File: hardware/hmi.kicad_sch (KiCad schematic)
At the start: 21 parts, among them J4 Conn_01x08, Q1 PNP, Q2 NPN, SW1 SW_Push, SW2 SW_Push, SW3 SW_Push, SW4 SW_Push, SW5 SW_Push, SW6 SW_Push, SW7 SW_Push, U8 PCF8574

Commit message: Second revision of schematic
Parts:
- removed C12: 4u7, symbol Device:C
- removed RN1: 9 x 10k, Resistor_THT:R_Array_SIP10, symbol Device:R_Network09
- removed U8: PCF8574, symbol Interface_Expansion:PCF8574
- added C12: 4u7, Capacitor_THT:CP_Radial_D4.0mm_P2.00mm, symbol Device:C_Polarized
- added J4, J5: Conn_01x07, Connector_PinHeader_2.54mm:PinHeader_1x07_P2.54mm_Vertical, symbol Connector_Generic:Conn_01x07
- added U8: PCF8574T, Package_SO:SOIC-16W_7.5x10.3mm_P1.27mm, symbol Interface_Expansion:PCF8574T
- BZ1: footprint (none) -> Connector_PinHeader_2.54mm:PinHeader_1x02_P2.54mm_Vertical
- D5: renamed from D4; footprint (none) -> LED_SMD:LED_1206_3216Metric
- J6: renamed from J4; footprint (none) -> Connector_PinHeader_2.54mm:PinHeader_1x08_P2.54mm_Vertical
- Q1, Q2: footprint (none) -> Package_TO_SOT_SMD:SOT-23
- R24: renamed from R22; footprint (none) -> Resistor_SMD:R_0603_1608Metric
- R25: renamed from R24; footprint (none) -> Resistor_SMD:R_0603_1608Metric
- R26: renamed from R23; footprint (none) -> Resistor_SMD:R_0603_1608Metric
- R27: renamed from R25; footprint (none) -> Resistor_SMD:R_0603_1608Metric
- R28: renamed from R26; footprint (none) -> Resistor_SMD:R_0603_1608Metric
- RV1: footprint (none) -> Potentiometer_SMD:Potentiometer_Vishay_TS53YJ_Vertical
- SW2: renamed from SW1; footprint (none) -> Button_Switch_SMD:SW_SPST_TL3342
- SW3: renamed from SW2; footprint (none) -> Button_Switch_SMD:SW_SPST_TL3342
- SW4: renamed from SW3; footprint (none) -> Button_Switch_SMD:SW_SPST_TL3342
- SW5: renamed from SW4; footprint (none) -> Button_Switch_SMD:SW_SPST_TL3342
- SW6: renamed from SW5; footprint (none) -> Button_Switch_SMD:SW_SPST_TL3342
- SW7: renamed from SW6; footprint (none) -> Button_Switch_SMD:SW_SPST_TL3342
- SW8: renamed from SW7; footprint (none) -> Button_Switch_SMD:SW_SPST_TL3342
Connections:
- net +5V is gone; now on net GND: D5.1 (K)
- net +3.3V: now also U8.16 (VDD)
- net A_Button: now also J5.1 (Pin_1)
- net B_Button: now also J5.2 (Pin_2)
- net C_Button: now also J5.3 (Pin_3)
- net GND: now also C12.2, U8.1 (A0), U8.2 (A1), U8.3 (A2), U8.8 (GND)
- net LCD_RST: now also C12.1
- net Left_Button: now also J5.5 (Pin_5)
- net POWER_EN: now also U8.4 (P0)
- net Right_Button: now also J5.4 (Pin_4)
- net SCL: now also U8.14 (SCL)
- net SDA: now also U8.15 (SDA)
- net Down renamed Down_Button
- net Down_Button: now also J5.6 (Pin_6)
- net UP renamed UP_Button
- net UP_Button: now also J5.7 (Pin_7)
- new net A_Button_CONN: J4.1 (Pin_1), U8.5 (P1)
- new net B_Button_CONN: J4.2 (Pin_2), U8.6 (P2)
- new net C_Button_CONN: J4.3 (Pin_3), U8.7 (P3)
- new net Down_Button_CONN: J4.6 (Pin_6), U8.11 (P6)
- new net Left_Button_CONN: J4.5 (Pin_5), U8.10 (P5)
- new net Right_Button_CONN: J4.4 (Pin_4), U8.9 (P4)
- new net UP_Button_CONN: J4.7 (Pin_7), U8.12 (P7)
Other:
- moved on the sheet: D5, J6, Q1, R25, R26, R27

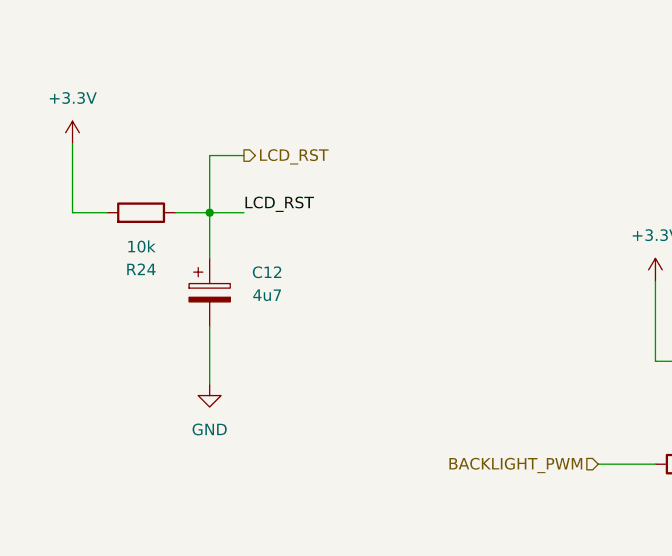
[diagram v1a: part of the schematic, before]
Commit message: Initial PCB placement and some schematic changes
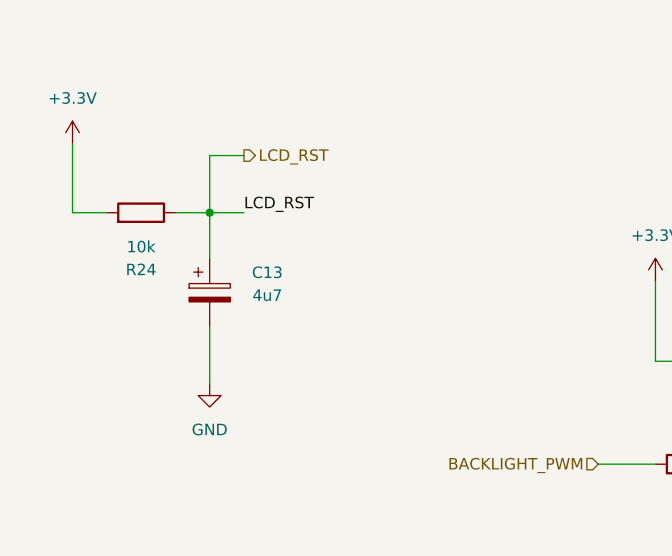
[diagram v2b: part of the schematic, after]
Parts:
- D5: footprint LED_SMD:LED_1206_3216Metric -> Diode_SMD:D_0603_1608Metric_Pad1.05x0.95mm_HandSolder
- renumbered C12 to C13
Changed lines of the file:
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@@
 			)
 		)
-		(property "Footprint" "LED_SMD:LED_1206_3216Metric"
+		(property "Footprint" "Diode_SMD:D_0603_1608Metric_Pad1.05x0.95mm_HandSolder"
 			(at 140.97 153.67 0)
 			(effects
@@
 		(on_board yes)
 		(dnp no)
-		(property "Reference" "C12"
+		(property "Reference" "C13"
 			(at 58.4835 49.8475 0)
 			(effects
@@
 			(project "esp8266_pygame"
 				(path "/fc3c54fb-6d1c-4231-9293-8fcb9c0b9706/4d35df8b-f9a9-4663-8ccd-4f07537e2734"
-					(reference "C12")
-					(unit 1)
-				)
+					(reference "C13")
+					(unit 1)
+				)

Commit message: Fixed keypad connector
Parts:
- removed J4, J5: Conn_01x07, Connector_PinHeader_2.54mm:PinHeader_1x07_P2.54mm_Vertical, symbol Connector_Generic:Conn_01x07
- added J4, J5: Conn_01x08, Connector_PinSocket_2.54mm:PinSocket_1x08_P2.54mm_Vertical, symbol Connector_Generic:Conn_01x08
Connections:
- net A_Button: now also J5.1 (Pin_1)
- net A_Button_CONN: now also J4.1 (Pin_1)
- net B_Button: now also J5.2 (Pin_2)
- net B_Button_CONN: now also J4.2 (Pin_2)
- net C_Button: now also J5.3 (Pin_3)
- net C_Button_CONN: now also J4.3 (Pin_3)
- net Down_Button: now also J5.6 (Pin_6)
- net Down_Button_CONN: now also J4.6 (Pin_6)
- net GND: now also J4.8 (Pin_8); no longer SW2.2, SW3.2, SW4.2, SW5.2, SW6.2, SW7.2, SW8.2
- net Left_Button: now also J5.5 (Pin_5)
- net Left_Button_CONN: now also J4.5 (Pin_5)
- net Right_Button: now also J5.4 (Pin_4)
- net Right_Button_CONN: now also J4.4 (Pin_4)
- net UP_Button: now also J5.7 (Pin_7)
- net UP_Button_CONN: now also J4.7 (Pin_7)
- new net BTN_GND: J5.8 (Pin_8), SW2.2, SW3.2, SW4.2, SW5.2, SW6.2, SW7.2, SW8.2

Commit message: Audio improvements
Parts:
- removed Q2: NPN, Package_TO_SOT_SMD:SOT-23, symbol Simulation_SPICE:NPN
- added C13: 100n, Capacitor_SMD:C_0603_1608Metric, symbol Device:C
- added C14: 10n, Capacitor_SMD:C_0603_1608Metric, symbol Device:C
- added C15: 10u, Capacitor_THT:CP_Radial_D4.0mm_P2.00mm, symbol Device:C_Polarized
- added C16: 47n, Capacitor_SMD:C_0603_1608Metric, symbol Device:C
- added C17: 220u, Capacitor_THT:CP_Radial_D4.0mm_P2.00mm, symbol Device:C_Polarized
- added R29: 10k, Resistor_SMD:R_0603_1608Metric, symbol Device:R
- added R30: 10, Resistor_SMD:R_0603_1608Metric, symbol Device:R
- added U9: LM386, Package_SO:SO-8_3.9x4.9mm_P1.27mm, symbol Amplifier_Audio:LM386
- renumbered C13 to C12
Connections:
- net +3.3V: no longer BZ1.1 (-)
- net BTN_GND: now also J5.5 (Pin_5); no longer J5.8 (Pin_8)
- net BUZZER: now also R28.1; no longer RV1.2
- net GND: now also BZ1.2 (+), J4.5 (Pin_5), C13.1, C14.1, R30.2, U9.2 (-), U9.4 (GND); no longer J4.8 (Pin_8)
- net Left_Button: now also J5.8 (Pin_8); no longer J5.5 (Pin_5)
- net Left_Button_CONN: now also J4.8 (Pin_8); no longer J4.5 (Pin_5)
- net at RV1.3: now also U9.3 (+); no longer R28.1
- net at R28.2: now also C13.2, R29.1
- new net: C14.2, R29.2, RV1.2
- new net: C16.2, C17.1, U9.5
- new net: BZ1.1 (-), C17.2
- new net: C15.1, U9.1 (GAIN)
- new net: C15.2, U9.8 (GAIN)
- new net: C16.1, R30.1
- new net +5V: U9.6 (V+)
- no-connect marks 1 -> 2
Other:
- moved on the sheet: BZ1, RV1

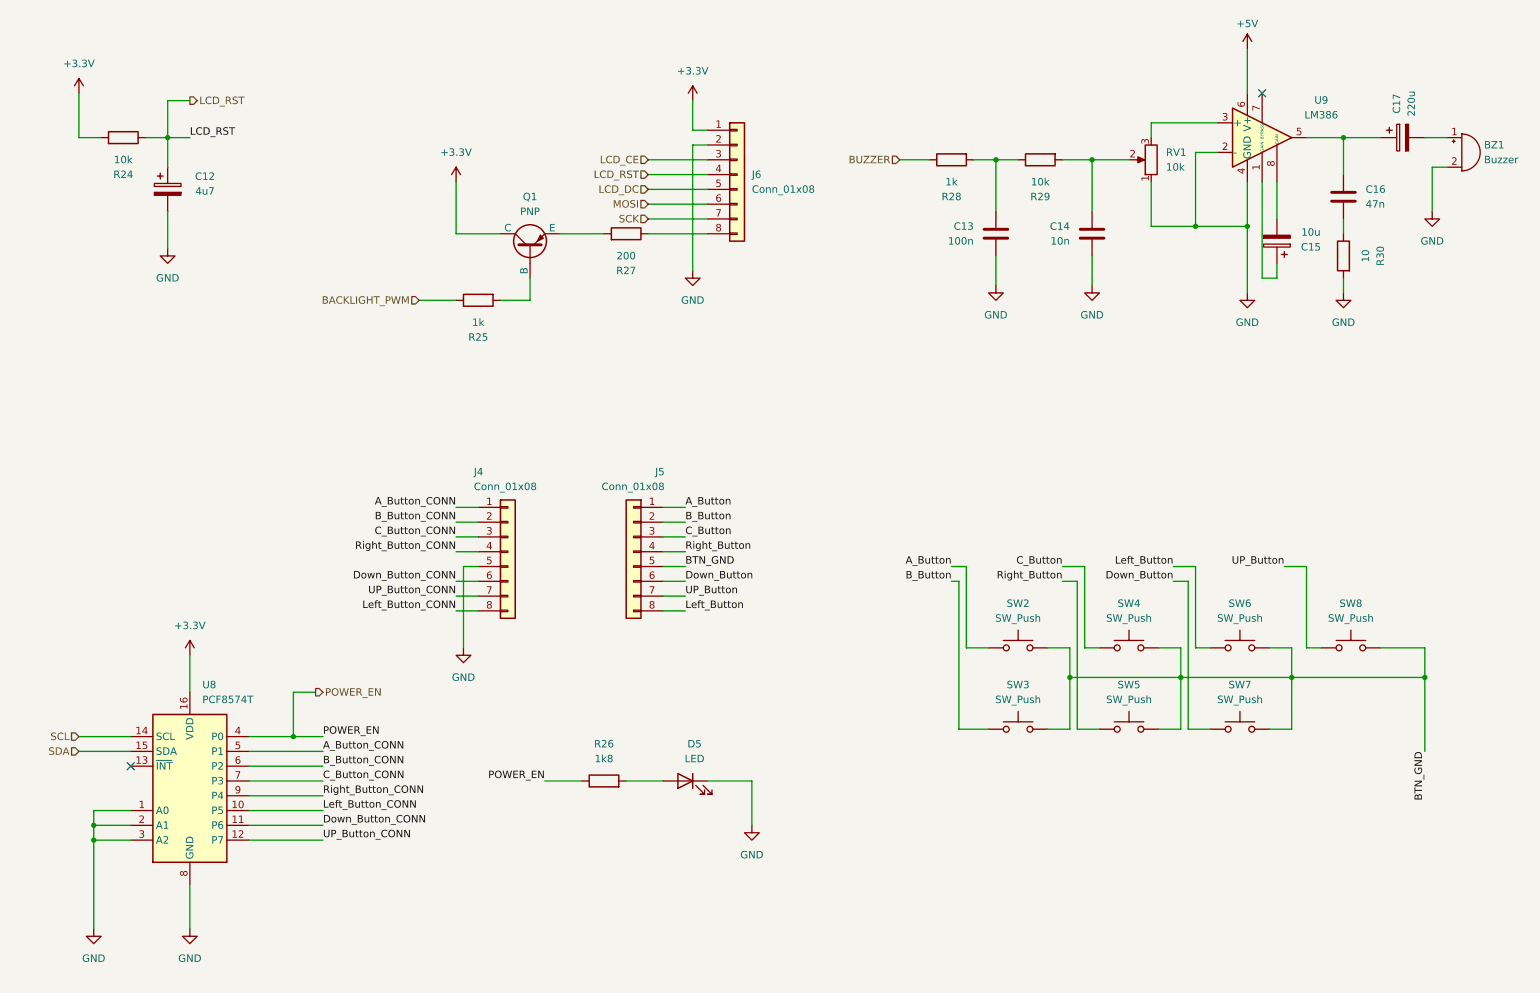
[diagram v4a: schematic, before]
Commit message: Fixed power enable bypass
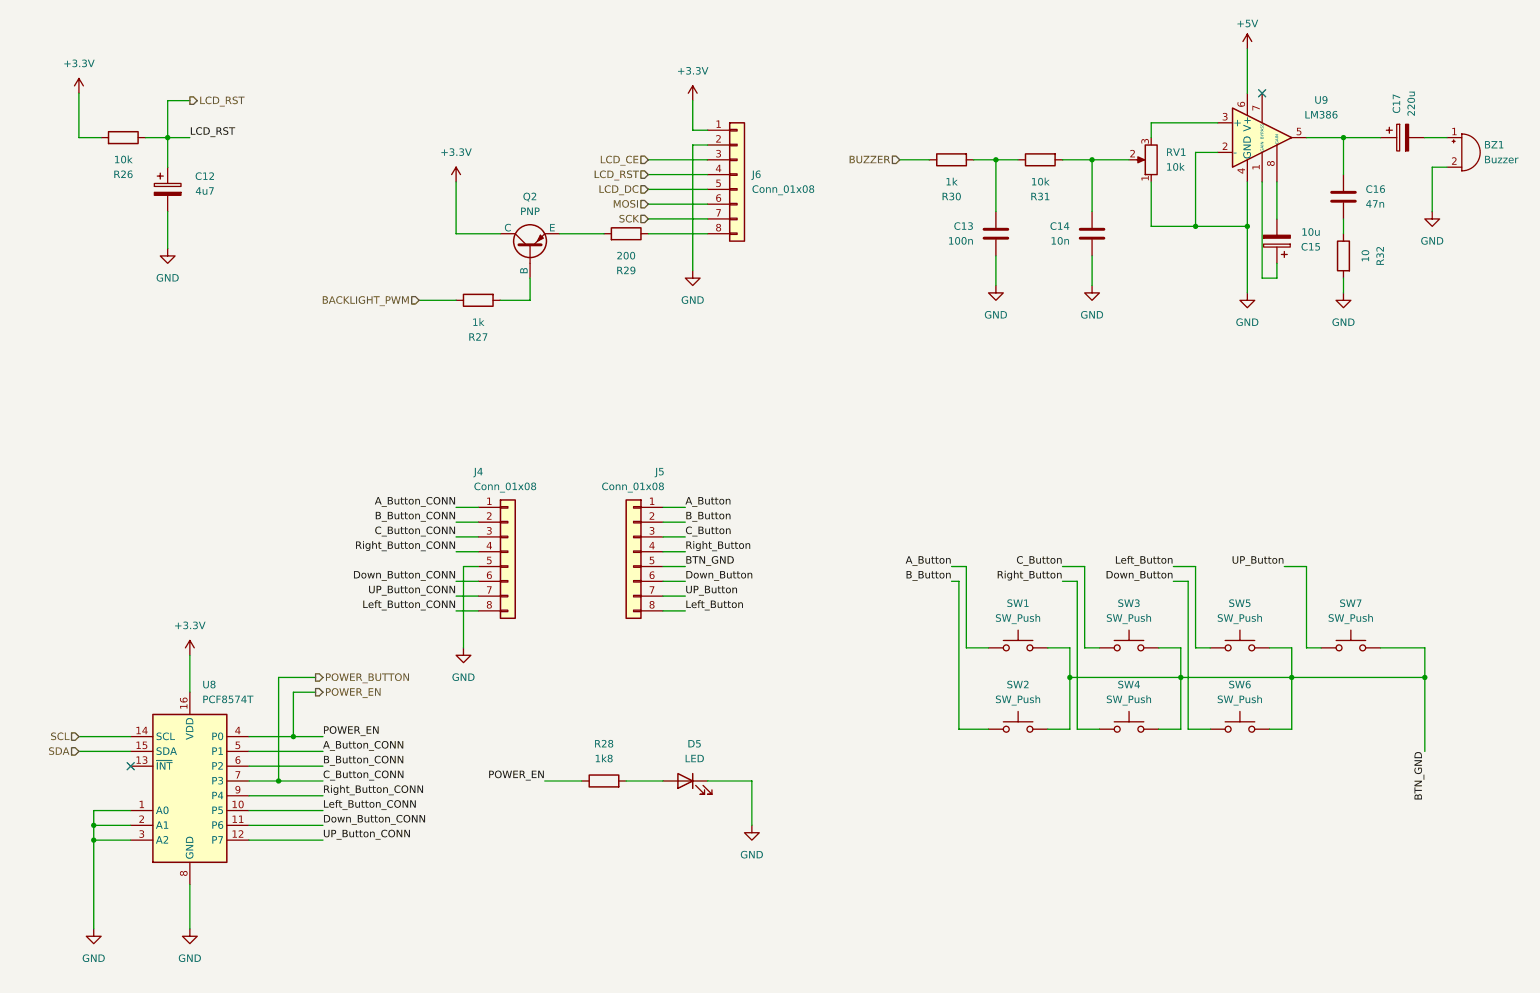
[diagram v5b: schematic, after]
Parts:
- renumbered Q1 to Q2, R24 to R26, R25 to R27, R26 to R28, R27 to R29, R28 to R30, R29 to R31, R30 to R32, SW2 to SW1, SW3 to SW2, SW4 to SW3, SW5 to SW4, SW6 to SW5, SW7 to SW6, SW8 to SW7
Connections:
- net C_Button_CONN renamed POWER_BUTTON
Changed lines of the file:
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@@
 	)
 	(junction
+		(at 71.12 153.67)
+		(diameter 0)
+		(color 0 0 0 0)
+	)
+	(junction
 		(at 73.66 146.05)
 		(diameter 0)
@@
 	(wire
 		(pts
+			(xy 71.12 153.67) (xy 78.74 153.67)
+		)
+		(stroke
+			(width 0)
+			(type default)
+		)
+	)
+	(wire
+		(pts
 			(xy 144.78 41.91) (xy 142.24 41.91)
 		)
@@
 	(wire
 		(pts
+			(xy 71.12 135.89) (xy 71.12 153.67)
+		)
+		(stroke
+			(width 0)
+			(type default)
+		)
+	)
+	(wire
+		(pts
 			(xy 232.41 45.72) (xy 228.6 45.72)
 		)
@@
 	(wire
 		(pts
+			(xy 77.47 135.89) (xy 71.12 135.89)
+		)
+		(stroke
+			(width 0)
+			(type default)
+		)
+	)
+	(wire
+		(pts
 			(xy 144.78 153.67) (xy 152.4 153.67)
 		)
@@
 	(wire
 		(pts
-			(xy 66.04 153.67) (xy 78.74 153.67)
+			(xy 66.04 153.67) (xy 71.12 153.67)
 		)
 		(stroke
@@
 		)
 	)
+	(hierarchical_label "POWER_BUTTON"
+		(shape output)
+		(at 77.47 135.89 0)
+		(effects
+			(font
+				(size 1.27 1.27)
+			)
+			(justify left)
+		)
+	)
 	(hierarchical_label "POWER_EN"
 		(shape output)
@@
 		(dnp no)
 		(fields_autoplaced yes)
-		(property "Reference" "SW8"
+		(property "Reference" "SW7"
 			(at 255.27 123.19 0)
 			(effects
@@
 			(project "esp8266_pygame"
 				(path "/fc3c54fb-6d1c-4231-9293-8fcb9c0b9706/4d35df8b-f9a9-4663-8ccd-4f07537e2734"
-					(reference "SW8")
+					(reference "SW7")
 					(unit 1)
 				)
@@
 		(on_board yes)
 		(dnp no)
-		(property "Reference" "R29"
+		(property "Reference" "R31"
 			(at 201.93 53.34 90)
 			(effects
@@
 			(project "esp8266_pygame"
 				(path "/fc3c54fb-6d1c-4231-9293-8fcb9c0b9706/4d35df8b-f9a9-4663-8ccd-4f07537e2734"
-					(reference "R29")
+					(reference "R31")
 					(unit 1)
 				)
@@
 		(dnp no)
 		(fields_autoplaced yes)
-		(property "Reference" "SW5"
+		(property "Reference" "SW4"
 			(at 217.17 137.16 0)
 			(effects
@@
 			(project "esp8266_pygame"
 				(path "/fc3c54fb-6d1c-4231-9293-8fcb9c0b9706/4d35df8b-f9a9-4663-8ccd-4f07537e2734"
-					(reference "SW5")
+					(reference "SW4")
 					(unit 1)
 				)
@@
 		(dnp no)
 		(fields_autoplaced yes)
-		(property "Reference" "SW3"
+		(property "Reference" "SW2"
 			(at 198.12 137.16 0)
 			(effects
@@
 			(project "esp8266_pygame"
 				(path "/fc3c54fb-6d1c-4231-9293-8fcb9c0b9706/4d35df8b-f9a9-4663-8ccd-4f07537e2734"
-					(reference "SW3")
+					(reference "SW2")
 					(unit 1)
 				)
@@
 		(on_board yes)
 		(dnp no)
-		(property "Reference" "R25"
+		(property "Reference" "R27"
 			(at 105.41 77.47 90)
 			(effects
@@
 			(project "esp8266_pygame"
 				(path "/fc3c54fb-6d1c-4231-9293-8fcb9c0b9706/4d35df8b-f9a9-4663-8ccd-4f07537e2734"
-					(reference "R25")
+					(reference "R27")
 					(unit 1)
 				)
@@
 		(dnp no)
 		(fields_autoplaced yes)
-		(property "Reference" "SW2"
+		(property "Reference" "SW1"
 			(at 198.12 123.19 0)
 			(effects
@@
 			(project "esp8266_pygame"
 				(path "/fc3c54fb-6d1c-4231-9293-8fcb9c0b9706/4d35df8b-f9a9-4663-8ccd-4f07537e2734"
-					(reference "SW2")
+					(reference "SW1")
 					(unit 1)
 				)
@@
 		(dnp no)
 		(fields_autoplaced yes)
-		(property "Reference" "Q1"
+		(property "Reference" "Q2"
 			(at 114.3 53.34 90)
 			(effects
@@
 			(project ""
 				(path "/fc3c54fb-6d1c-4231-9293-8fcb9c0b9706/4d35df8b-f9a9-4663-8ccd-4f07537e2734"
-					(reference "Q1")
+					(reference "Q2")
 					(unit 1)
 				)
@@
 		(on_board yes)
 		(dnp no)
-		(property "Reference" "R27"
+		(property "Reference" "R29"
 			(at 130.81 66.04 90)
 			(effects
@@
 			(project "esp8266_pygame"
 				(path "/fc3c54fb-6d1c-4231-9293-8fcb9c0b9706/4d35df8b-f9a9-4663-8ccd-4f07537e2734"
-					(reference "R27")
+					(reference "R29")
 					(unit 1)
 				)
@@
 		(on_board yes)
 		(dnp no)
-		(property "Reference" "R30"
+		(property "Reference" "R32"
 			(at 260.35 63.5 90)
 			(effects
@@
 			(project "esp8266_pygame"
 				(path "/fc3c54fb-6d1c-4231-9293-8fcb9c0b9706/4d35df8b-f9a9-4663-8ccd-4f07537e2734"
-					(reference "R30")
+					(reference "R32")
 					(unit 1)
 				)
@@
 		(dnp no)
 		(fields_autoplaced yes)
-		(property "Reference" "SW6"
+		(property "Reference" "SW5"
 			(at 236.22 123.19 0)
 			(effects
@@
 			(project "esp8266_pygame"
 				(path "/fc3c54fb-6d1c-4231-9293-8fcb9c0b9706/4d35df8b-f9a9-4663-8ccd-4f07537e2734"
-					(reference "SW6")
+					(reference "SW5")
 					(unit 1)
 				)
@@
 		(on_board yes)
 		(dnp no)
-		(property "Reference" "R28"
+		(property "Reference" "R30"
 			(at 186.69 53.34 90)
 			(effects
@@
 			(project "esp8266_pygame"
 				(path "/fc3c54fb-6d1c-4231-9293-8fcb9c0b9706/4d35df8b-f9a9-4663-8ccd-4f07537e2734"
-					(reference "R28")
+					(reference "R30")
 					(unit 1)
 				)
@@
 		(dnp no)
 		(fields_autoplaced yes)
-		(property "Reference" "SW7"
+		(property "Reference" "SW6"
 			(at 236.22 137.16 0)
 			(effects
@@
 			(project "esp8266_pygame"
 				(path "/fc3c54fb-6d1c-4231-9293-8fcb9c0b9706/4d35df8b-f9a9-4663-8ccd-4f07537e2734"
-					(reference "SW7")
+					(reference "SW6")
 					(unit 1)
 				)
@@
 		(on_board yes)
 		(dnp no)
-		(property "Reference" "R24"
+		(property "Reference" "R26"
 			(at 44.45 49.53 90)
 			(effects
@@
 			(project "esp8266_pygame"
 				(path "/fc3c54fb-6d1c-4231-9293-8fcb9c0b9706/4d35df8b-f9a9-4663-8ccd-4f07537e2734"
-					(reference "R24")
+					(reference "R26")
 					(unit 1)
 				)
@@
 		(dnp no)
 		(fields_autoplaced yes)
-		(property "Reference" "SW4"
+		(property "Reference" "SW3"
 			(at 217.17 123.19 0)
 			(effects
@@
 			(project "esp8266_pygame"
 				(path "/fc3c54fb-6d1c-4231-9293-8fcb9c0b9706/4d35df8b-f9a9-4663-8ccd-4f07537e2734"
-					(reference "SW4")
+					(reference "SW3")
 					(unit 1)
 				)
@@
 		(dnp no)
 		(fields_autoplaced yes)
-		(property "Reference" "R26"
+		(property "Reference" "R28"
 			(at 127 147.32 90)
 			(effects
@@
 			(project "esp8266_pygame"
 				(path "/fc3c54fb-6d1c-4231-9293-8fcb9c0b9706/4d35df8b-f9a9-4663-8ccd-4f07537e2734"
-					(reference "R26")
+					(reference "R28")
 					(unit 1)
 				)
